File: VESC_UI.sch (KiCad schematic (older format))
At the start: 60 parts, among them J1 Hall_SS443A, J2 Hall_SS443A, J3 Conn_01x07_Male, J4 Conn_01x09_Female, J5 Conn_01x05_Male, J6 Conn_01x04_Male, J8 Conn_01x02_Male, J9 Conn_01x02_Male, Q1 Q_0010-DVB_Q, Q2 Q_0010-DVB_Q, SW1 SW_Push, SW2 SW_Push, SW3 SW_Push, SW4 SW_Push, SW5 SW_Push, U2 STM32F401CEUx, U3 M95M04-DR, Y1 Crystal_GND24_Small

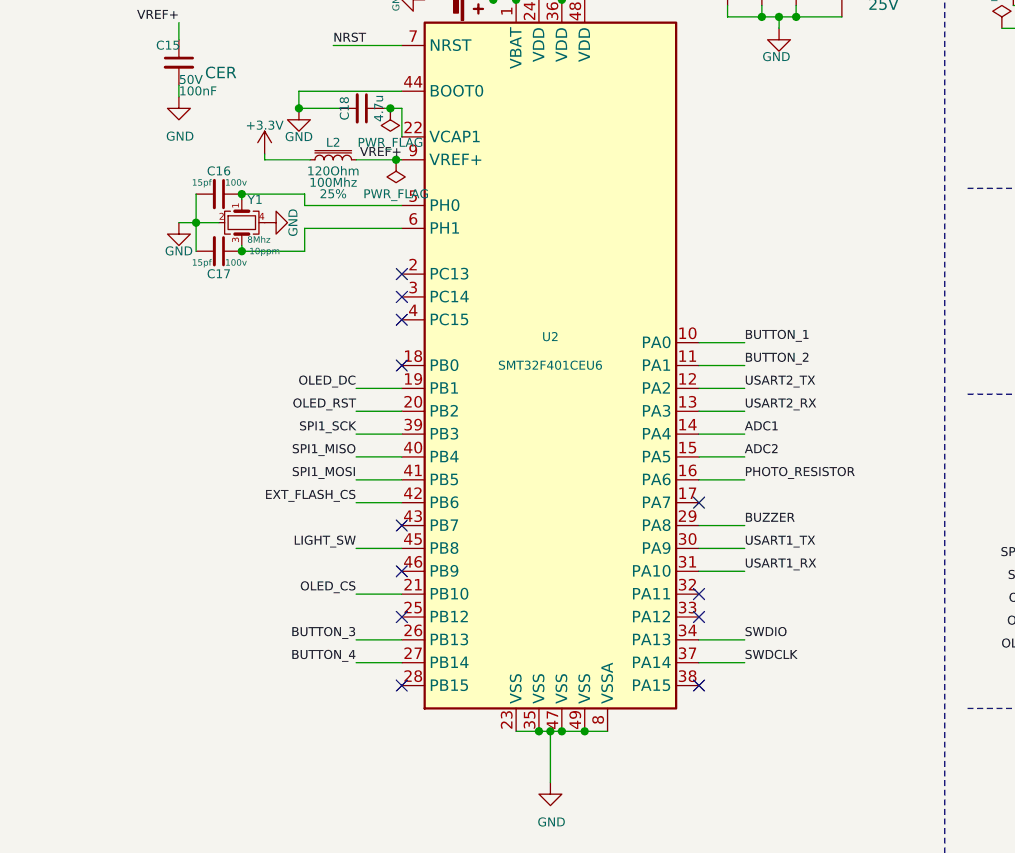
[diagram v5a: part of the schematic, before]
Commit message: fix and refactor: both mainboard and screenboard
Many improvements made
- Fixed all issues with footprints
- Optimized components placement and tracks
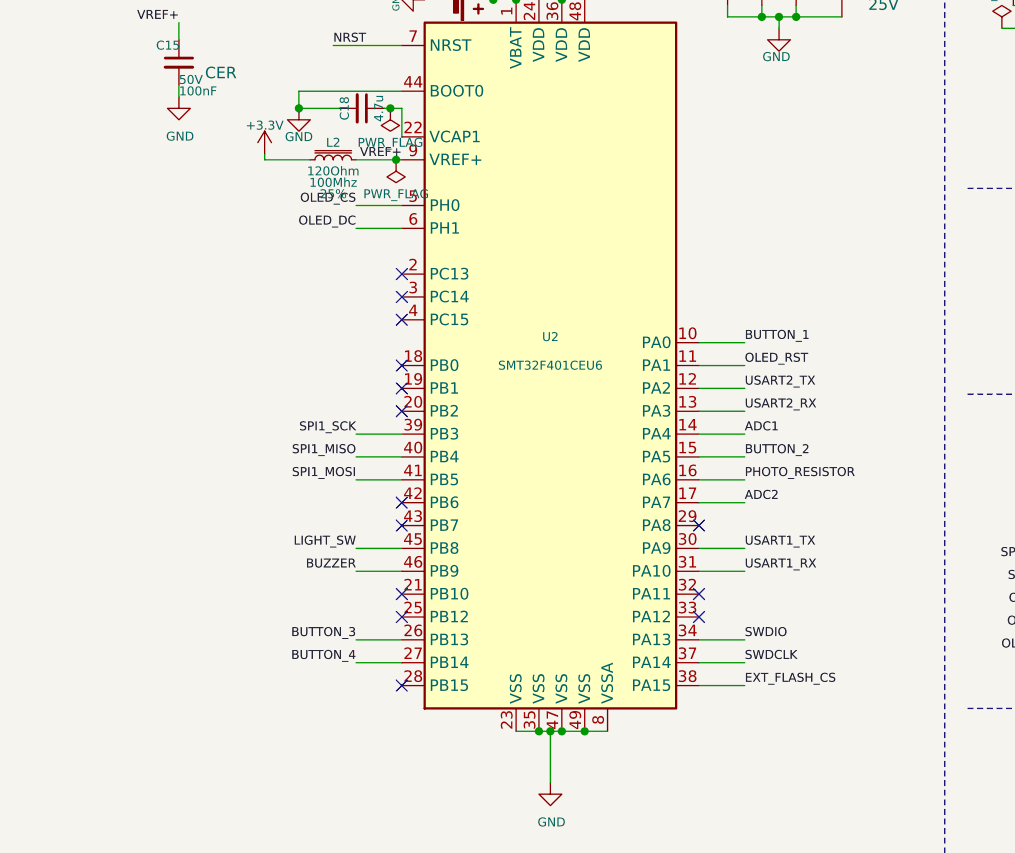
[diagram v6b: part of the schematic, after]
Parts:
- removed C16, C17: C_Small, Capacitor_SMD:C_0603_1608Metric_Pad1.05x0.95mm_HandSolder, symbol Device:C_Small
- removed Y1: Crystal_GND24_Small, Crystal:Crystal_SMD_Abracon_ABM3B-4Pin_5.0x3.2mm, symbol Device:Crystal_GND24_Small
- R13: footprint Resistor_THT:R_Axial_DIN0204_L3.6mm_D1.6mm_P2.54mm_Vertical -> OptoDevice:R_LDR_4.9x4.2mm_P2.54mm_Vertical
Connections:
- net ADC2: now also U2.17 (PA7); no longer U2.15 (PA5)
- net BUTTON_2: now also U2.15 (PA5); no longer U2.11 (PA1)
- net BUZZER: now also U2.46 (PB9); no longer U2.29 (PA8)
- net EXT_FLASH_CS: now also U2.38 (PA15); no longer U2.42 (PB6)
- net OLED_CS: now also U2.5 (PH0); no longer U2.21 (PB10)
- net OLED_DC: now also U2.6 (PH1); no longer U2.19 (PB1)
- net OLED_RST: now also U2.11 (PA1); no longer U2.20 (PB2)
- no-connect marks 12 -> 14
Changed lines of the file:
@@
 Wire Wire Line
 	8175 4225 8225 4225
-$Comp
-L power:GND #PWR031
-U 1 1 5F5E2B52
-P 6550 2000
-F 0 "#PWR031" H 6550 1750 39  0001 C CNN
-F 1 "GND" H 6550 1875 39  0000 C CNN
-F 2 "" H 6550 2000 39  0001 C CNN
-F 3 "" H 6550 2000 39  0001 C CNN
-	1    6550 2000
-	1    0    0    -1
-$EndComp
 NoConn ~ 7525 2225
 Wire Wire Line
@@
 F 0 "R13" H 2520 6846 39  0000 L CNN
 F 1 "R_PHOTO" H 2520 6755 39  0000 L CNN
-F 2 "Resistor_THT:R_Axial_DIN0204_L3.6mm_D1.6mm_P2.54mm_Vertical" V 2500 6550 39  0001 L CNN
+F 2 "OptoDevice:R_LDR_4.9x4.2mm_P2.54mm_Vertical" V 2500 6550 39  0001 L CNN
 F 3 "~" H 2450 6750 39  0001 C CNN
 	1    2450 6800
@@
 	2450 6975 2450 6950
 NoConn ~ 7525 4025
-NoConn ~ 7525 3525
-NoConn ~ 8825 4025
+NoConn ~ 8825 3725
+NoConn ~ 7525 3225
 $Comp
 L Connector:Conn_01x04_Male J6
@@
 	0    1    1    0
 $EndComp
-Wire Wire Line
-	7100 1925 7100 1875
 $Comp
 L power:+3.3V #PWR032
@@
 	6550 1450 6550 1400
 $Comp
-L Device:Crystal_GND24_Small Y1
-U 1 1 5F7C9C16
-P 6825 2000
-F 0 "Y1" V 6725 2025 39  0000 L CNN
-F 1 "Crystal_GND24_Small" V 6862 2144 39  0001 L CNN
-F 2 "Crystal:Crystal_SMD_Abracon_ABM3B-4Pin_5.0x3.2mm" H 6825 2000 39  0001 C CNN
-F 3 "http://www.farnell.com/datasheets/2581422.pdf?_ga=2.29888511.1106248822.1601817720-706293543.1593275528&_gac=1.90918504.1601920666.CjwKCAjwiOv7BRBREiwAXHbv3Nre1ZRkFzw4o4_G1jayqOyIr5XBMbrn0P0vXxc_gtBymGv78yQuRBoCZ7kQAvD_BwE" H 6825 2000 39  0001 C CNN
-F 4 "8Mhz" V 6900 2075 28  0000 C CNN "Field4"
-F 5 "10ppm" V 6950 2100 28  0000 C CNN "Field5"
-	1    6825 2000
-	0    1    1    0
-$EndComp
-$Comp
-L Device:C_Small C16
-U 1 1 5F7DB934
-P 6725 1875
-F 0 "C16" V 6625 1875 39  0000 C CNN
-F 1 "C_Small" V 6587 1875 39  0001 C CNN
-F 2 "Capacitor_SMD:C_0603_1608Metric_Pad1.05x0.95mm_HandSolder" H 6725 1875 39  0001 C CNN
-F 3 "~" H 6725 1875 39  0001 C CNN
-F 4 "15pf" V 6675 1800 28  0000 C CNN "Field4"
-F 5 "100v" V 6675 1950 28  0000 C CNN "Field5"
-	1    6725 1875
-	0    1    1    0
-$EndComp
-$Comp
-L Device:C_Small C17
-U 1 1 5F7DEDB9
-P 6725 2125
-F 0 "C17" V 6825 2125 39  0000 C CNN
-F 1 "C_Small" V 6587 2125 39  0001 C CNN
-F 2 "Capacitor_SMD:C_0603_1608Metric_Pad1.05x0.95mm_HandSolder" H 6725 2125 39  0001 C CNN
-F 3 "~" H 6725 2125 39  0001 C CNN
-F 4 "15pf" V 6775 2050 28  0000 C CNN "Field4"
-F 5 "100v" V 6775 2200 28  0000 C CNN "Field5"
-	1    6725 2125
-	0    1    1    0
-$EndComp
-$Comp
-L power:GND #PWR033
-U 1 1 5F8237D6
-P 6925 2000
-F 0 "#PWR033" H 6925 1750 39  0001 C CNN
-F 1 "GND" H 6925 1875 39  0000 C CNN
-F 2 "" H 6925 2000 39  0001 C CNN
-F 3 "" H 6925 2000 39  0001 C CNN
-	1    6925 2000
-	0    -1   -1   0
-$EndComp
-Wire Wire Line
-	6825 1875 6825 1900
-Wire Wire Line
-	6825 2125 6825 2100
-Wire Wire Line
-	6625 1875 6625 2000
-Wire Wire Line
-	6625 2000 6725 2000
-Connection ~ 6625 2000
-Wire Wire Line
-	6625 2000 6625 2125
-Wire Wire Line
-	6625 2000 6550 2000
-Wire Wire Line
-	7100 2125 6825 2125
-Wire Wire Line
-	7100 2025 7100 2125
-Connection ~ 6825 2125
-Wire Wire Line
-	6825 1875 7100 1875
-Connection ~ 6825 1875
-Wire Wire Line
-	7525 1925 7100 1925
-Wire Wire Line
-	7100 2025 7525 2025
-$Comp
 L Device:R R6
 U 1 1 5F920E7A
@@
 Wire Wire Line
 	1875 6750 1875 6700
-Text Label 9025 2625 0    39   ~ 0
+Text Label 9025 3025 0    39   ~ 0
 BUTTON_2
 Text Label 7325 3825 2    39   ~ 0
@@
 Text Label 9025 2525 0    39   ~ 0
 BUTTON_1
-Text Label 7325 3625 2    39   ~ 0
+Text Label 7325 1925 2    39   ~ 0
 OLED_CS
-Text Label 7325 2725 2    39   ~ 0
+Text Label 7325 2025 2    39   ~ 0
 OLED_DC
 Text Label 7325 2925 2    39   ~ 0
@@
 Text Label 9025 2925 0    39   ~ 0
 ADC1
-Text Label 9025 3025 0    39   ~ 0
+Text Label 9025 3225 0    39   ~ 0
 ADC2
 Text Label 9025 3125 0    39   ~ 0
@@
 Text Label 7325 3425 2    39   ~ 0
 LIGHT_SW
-Text Label 7325 2825 2    39   ~ 0
+Text Label 9025 2625 0    39   ~ 0
 OLED_RST
 Text Label 950  3075 2    39   ~ 0
@@
 	1    0    0    -1
 $EndComp
-Text Label 9025 3325 0    39   ~ 0
+Text Label 7325 3525 2    39   ~ 0
 BUZZER
 Text Label 3000 2925 2    39   ~ 0
@@
 	10575 4950 10675 4950
 Wire Wire Line
-	7525 2725 7325 2725
-Wire Wire Line
 	7325 3025 7525 3025
-Wire Wire Line
-	7525 2825 7325 2825
-NoConn ~ 8825 3225
 Text Label 7325 3025 2    39   ~ 0
 SPI1_MISO
@@
 Text Label 8675 5425 0    39   ~ 0
 SPI1_SCK
-Text Label 7325 3225 2    39   ~ 0
+Text Label 9025 4025 0    39   ~ 0
 EXT_FLASH_CS
 Text Label 7875 5625 2    39   ~ 0
@@
 Connection ~ 10450 1150
 NoConn ~ 8825 3625
-NoConn ~ 8825 3725
+NoConn ~ 8825 3325
 NoConn ~ 7525 3325
 NoConn ~ 7525 3725
-Wire Wire Line
-	7325 3225 7525 3225
-Wire Wire Line
-	7525 3625 7325 3625
-Wire Wire Line
-	9025 2625 8825 2625
-Wire Wire Line
-	8825 3325 9025 3325
 Wire Notes Line
 	4550 3600 525  3600
@@
 	1    0    0    -1
 $EndComp
+Wire Wire Line
+	9025 4025 8825 4025
+Wire Wire Line
+	7525 3525 7325 3525
+Wire Wire Line
+	8825 3225 9025 3225
+NoConn ~ 7525 3625
+Wire Wire Line
+	7525 1925 7325 1925
+Wire Wire Line
+	7525 2025 7325 2025
+NoConn ~ 7525 2725
+NoConn ~ 7525 2825
+Wire Wire Line
+	8825 2625 9025 2625
 $EndSCHEMATC

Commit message: Finalize new board
- Remove some useless components
- Change some footprints according to components availability
- Optimize tracks and placements
- Fix bad LDR and screen location
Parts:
- C1: value C_Small -> 10n; Field4 10nF -> (none); Tolerance (none) -> 10%; Voltage (none) -> 50V
- C10, C9: value C_Small -> 100n; Dielectric (none) -> X5R; Field4 100nF -> (none); Voltage (none) -> 50V
- C12: value C_0033 -> 100n; Dielectric (none) -> X5R; Field5 100nF -> (none); Field6 16V -> (none); Field7 X5R -> (none); Field8 10% -> (none); Tolerance (none) -> 10%; Voltage (none) -> 50V
- C15, C24: value C_0033 -> 100n; Dielectric (none) -> X5R; Field4 CER -> (none); Field5 100nF -> (none); Field6 50V -> (none); Field7 X5R -> (none); Field8 10% -> (none); Voltage (none) -> 50V
- C19, C20, C21: value C_Small -> 100n; Dielectric (none) -> X5R; Field4 100n -> (none); Voltage (none) -> 50V
- C2: value C_0003-DVB_C -> 10µF; Dielectric (none) -> X7R; Field5 10µF -> (none); Field6 25V -> (none); Field7 X5R -> (none); Field8 10% -> (none); Tolerance (none) -> 10%; Voltage (none) -> 25V
- C22: value CP_Small -> SUpercap 330mF
- C23: value C_0033 -> 100n; Dielectric (none) -> X5R; Field5 100nF -> (none); Field6 50V -> (none); Field7 X5R -> (none); Field8 10% -> (none); Tolerance (none) -> 10%; Voltage (none) -> 50V
- C6: value C_Small -> 100n; Dielectric (none) -> X5R; Field4 100nF -> (none); Tolerance (none) -> 10%; Voltage (none) -> 50V
- D1, D2, D3, D4, D5, D6: value LED_Small_ALT -> LED 5mm - White
- D10: value D_Schottky_Small_ALT -> Schottky CD0603-B0240R
- J1, J2: value Hall_SS443A -> Hall_SS441R
- L2: value MMZ1608B121C -> MMZ1608B121CTDH5; Field4 120Ohm -> 120 Ohm
- Q1: value Q_0010-DVB_Q -> Mosfet IRLML2060TRPBF; symbol VESC_UI-rescue:Q_0010-DVB_Q -> Transistor_FET:IRLML2060; Field5 50Vds -> 20Vds; Field6 220mA -> 1.2A
- Q2: value Q_0010-DVB_Q -> Mosfet IRLML2060TRPBF; symbol VESC_UI-rescue:Q_0010-DVB_Q -> Transistor_FET:IRLML2060; Field6 320mA -> 1.2A; Field8 BSS138PW -> (none)
- R1, R4, R6: value R_0020 -> 30; Field4 30 -> (none); Field5 1% -> (none); Field6 100mW -> (none); Precision (none) -> 1%
- R12, R3, R5, R7, R9: value R_Small -> 100; Field4 100 -> (none); Precision (none) -> 1%
- R13: value R_PHOTO -> NSL-19M51
- R14: value R_0020 -> 10k; Field4 10k -> (none); Field5 1% -> (none); Field6 100mW -> (none); Precision (none) -> 1%
- R17, R18: value R_Small -> 0; Field4 0 -> (none)
- R2: value R_0020 -> 100k; Field4 100k -> (none); Field5 1% -> (none); Field6 100mW -> (none); Precision (none) -> 1%
- R21, R22: value R_Small -> 10k; Field4 10k -> (none); Precision (none) -> 1%
- R8: value R_Small -> 1M; Field4 1M -> (none); Field5 1% -> (none); Precision (none) -> 1%
- SW1, SW2, SW3, SW4: value SW_Push -> Vertical push button
- SW5: value SW_Push -> Push button; footprint Button_Switch_SMD:SW_SPST_TL3305A -> Button_Switch_SMD:SW_SPST_B3U-1000P-B
- U2: value STM32F401CEUx -> STM32F401CEU6
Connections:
- net +5V: now also C6.2; no longer C6.1
- net GND: now also C6.1; no longer C6.2
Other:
- moved on the sheet: C1, R2, R8

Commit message: Finalized PCBs
- Add MicroSD Card support on screen board
- Fix Hall sensors footprints (flip board side)
- Change screen connector
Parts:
- J4: value Conn_01x09_Female -> Conn_02x05_Female; footprint Connector_PinHeader_2.00mm:PinHeader_1x09_P2.00mm_Vertical -> Connector_PinSocket_2.00mm:PinSocket_2x05_P2.00mm_Vertical; symbol Connector:Conn_01x09_Female -> Connector_Generic:Conn_02x05_Odd_Even
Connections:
- net +3V3: now also J4.2 (Pin_2); no longer J4.3 (Pin_3)
- net +5V: no longer J4.2 (Pin_2)
- net GND: now also J4.3 (Pin_3); no longer J4.4 (Pin_4)
- net OLED_CS: now also J4.8 (Pin_8); no longer J4.7 (Pin_7)
- net OLED_DC: now also J4.7 (Pin_7); no longer J4.8 (Pin_8)
- net SPI1_MISO: now also J4.5 (Pin_5)
- net SPI1_MOSI: now also J4.4 (Pin_4); no longer J4.5 (Pin_5)
- net SD_CS: now reaches U2.42 (PB6)
- net SD_CS: now also J4.10 (Pin_10)
- no-connect marks 14 -> 13
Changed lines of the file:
@@
 NoConn ~ 7525 4025
 NoConn ~ 8825 3725
-NoConn ~ 7525 3225
 $Comp
 L Connector:Conn_01x04_Male J6
@@
 	2525 1925 2525 3600
 $Comp
-L Connector:Conn_01x09_Female J4
+L Connector_Generic:Conn_02x05_Odd_Even J4
 U 1 1 5FD97606
-P 10800 3475
-F 0 "J4" H 10828 3501 50  0000 L CNN
-F 1 "Conn_01x09_Female" H 10828 3410 50  0000 L CNN
-F 2 "Connector_PinHeader_2.00mm:PinHeader_1x09_P2.00mm_Vertical" H 10800 3475 50  0001 C CNN
-F 3 "~" H 10800 3475 50  0001 C CNN
-	1    10800 3475
+P 10475 3425
+F 0 "J4" H 10475 3425 50  0000 L CNN
+F 1 "Conn_02x05_Female" H 10175 3100 50  0000 L CNN
+F 2 "Connector_PinSocket_2.00mm:PinSocket_2x05_P2.00mm_Vertical" H 10475 3425 50  0001 C CNN
+F 3 "https://cdn.harwin.com/pdfs/M22-634.pdf" H 10475 3425 50  0001 C CNN
+	1    10475 3425
 	1    0    0    -1
 $EndComp
@@
 Connection ~ 10450 950
 $Comp
-L power:+5V #PWR0101
-U 1 1 5FDA4081
-P 10475 3175
-F 0 "#PWR0101" H 10475 3025 39  0001 C CNN
-F 1 "+5V" H 10400 3275 39  0000 C CNN
-F 2 "" H 10475 3175 39  0001 C CNN
-F 3 "" H 10475 3175 39  0001 C CNN
-	1    10475 3175
-	1    0    0    -1
-$EndComp
-Wire Wire Line
-	10600 3175 10475 3175
-$Comp
 L power:+12V #PWR0102
 U 1 1 5FDAD166
-P 10525 3075
-F 0 "#PWR0102" H 10525 2925 50  0001 C CNN
-F 1 "+12V" H 10450 3225 39  0000 C CNN
-F 2 "" H 10525 3075 50  0001 C CNN
-F 3 "" H 10525 3075 50  0001 C CNN
-	1    10525 3075
-	1    0    0    -1
-$EndComp
-Wire Wire Line
-	10600 3075 10525 3075
+P 10225 3150
+F 0 "#PWR0102" H 10225 3000 50  0001 C CNN
+F 1 "+12V" H 10325 3225 39  0000 C CNN
+F 2 "" H 10225 3150 50  0001 C CNN
+F 3 "" H 10225 3150 50  0001 C CNN
+	1    10225 3150
+	1    0    0    -1
+$EndComp
 $Comp
 L power:PWR_FLAG #FLG0105
 U 1 1 5FDB679E
-P 10600 3075
-F 0 "#FLG0105" H 10600 3150 39  0001 C CNN
-F 1 "PWR_FLAG" H 10775 3200 39  0000 C CNN
-F 2 "" H 10600 3075 39  0001 C CNN
-F 3 "~" H 10600 3075 39  0001 C CNN
-	1    10600 3075
-	1    0    0    -1
-$EndComp
-Connection ~ 10600 3075
+P 10150 3150
+F 0 "#FLG0105" H 10150 3225 39  0001 C CNN
+F 1 "PWR_FLAG" H 10050 3300 39  0000 C CNN
+F 2 "" H 10150 3150 39  0001 C CNN
+F 3 "~" H 10150 3150 39  0001 C CNN
+	1    10150 3150
+	1    0    0    -1
+$EndComp
 $Comp
 L power:+3.3V #PWR0103
 U 1 1 5FDB7952
-P 10425 3275
-F 0 "#PWR0103" H 10425 3125 39  0001 C CNN
-F 1 "+3.3V" H 10325 3375 39  0000 C CNN
-F 2 "" H 10425 3275 39  0001 C CNN
-F 3 "" H 10425 3275 39  0001 C CNN
-	1    10425 3275
-	1    0    0    -1
-$EndComp
-Wire Wire Line
-	10425 3275 10600 3275
+P 10775 3225
+F 0 "#PWR0103" H 10775 3075 39  0001 C CNN
+F 1 "+3.3V" H 10675 3325 39  0000 C CNN
+F 2 "" H 10775 3225 39  0001 C CNN
+F 3 "" H 10775 3225 39  0001 C CNN
+	1    10775 3225
+	1    0    0    -1
+$EndComp
 $Comp
 L power:GND #PWR0104
 U 1 1 5FDC13A0
-P 10600 3375
-F 0 "#PWR0104" H 10600 3125 39  0001 C CNN
-F 1 "GND" V 10605 3247 39  0000 R CNN
-F 2 "" H 10600 3375 39  0001 C CNN
-F 3 "" H 10600 3375 39  0001 C CNN
-	1    10600 3375
+P 10275 3325
+F 0 "#PWR0104" H 10275 3075 39  0001 C CNN
+F 1 "GND" V 10275 3225 39  0000 R CNN
+F 2 "" H 10275 3325 39  0001 C CNN
+F 3 "" H 10275 3325 39  0001 C CNN
+	1    10275 3325
 	0    1    1    0
 $EndComp
-Text Label 10425 3475 2    39   ~ 0
+Text Label 10775 3325 0    39   ~ 0
 SPI1_MOSI
-Text Label 10425 3575 2    39   ~ 0
+Text Label 10775 3425 0    39   ~ 0
 SPI1_SCK
-Text Label 10425 3675 2    39   ~ 0
+Text Label 10775 3525 0    39   ~ 0
 OLED_CS
-Text Label 10425 3775 2    39   ~ 0
+Text Label 10275 3525 2    39   ~ 0
 OLED_DC
-Text Label 10425 3875 2    39   ~ 0
+Text Label 10275 3625 2    39   ~ 0
 OLED_RST
-Wire Wire Line
-	10425 3875 10600 3875
-Wire Wire Line
-	10600 3775 10425 3775
-Wire Wire Line
-	10425 3675 10600 3675
-Wire Wire Line
-	10600 3575 10425 3575
-Wire Wire Line
-	10425 3475 10600 3475
 $Comp
 L VESC_UI-rescue:C_0003-DVB_C C2
@@
 	-1   0    0    1
 $EndComp
+Wire Wire Line
+	10275 3225 10225 3225
+Text Label 10275 3425 2    39   ~ 0
+SPI1_MISO
+Text Label 7325 3225 2    39   ~ 0
+SD_CS
+Wire Wire Line
+	7525 3225 7325 3225
+Text Label 10775 3625 0    39   ~ 0
+SD_CS
+Wire Wire Line
+	10225 3150 10225 3225
+Wire Wire Line
+	10150 3150 10150 3225
+Wire Wire Line
+	10150 3225 10225 3225
+Connection ~ 10225 3225
 $EndSCHEMATC
